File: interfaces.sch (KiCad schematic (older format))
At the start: 68 parts, among them J6 0878311420, J7 61300611121, U1 MTFC32GAPALBH-AIT, U14 XC7A100T-FGG484, U17 USB3300-EZK-TR, U18 USB3300-EZK-TR, U6 NVT2008DQ,115, Y1 TSX-3225, Y3 TSX-3225

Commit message: Replaced and connected eMMC, replaced RJ45
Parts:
- removed U1: MTFC32GAPALBH-AIT, antmicro-footprints:MICRON_EMMC_153, symbol antmicroMemory:MTFC32GAPALBH-AIT
- added U1: MTFC16GAPALNA-AIT, antmicro-footprints:BGA100CP100_17X10_1800X1400X140B46N, symbol antmicroMemory:MTFC16GAPALNA-AIT
- gave numbers to parts that had none: 1
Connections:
- wire segments 354 -> 358
- no-connect marks 11 -> 9
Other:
- note removed: "TODO: change to MTFC8GAMALNA which has 1mm ball pitch"
- moved on the sheet: C183, C184, C185, C186, C187, C188, C189, R116, R117, R118, R119, R120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

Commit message: Update RBIAS and filtering caps around ULPI USB controlers
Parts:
- removed C223, C224, C8, C9: C_4u7_0402, antmicro-footprints:0402-cap, symbol antmicroCapacitors0402:C_4u7_0402
- removed R5, R7: R_120k_0402, antmicro-footprints:0402-res, symbol antmicroResistors0402:R_120k_0402
- added R10, R11, R12, R9: R_0R_0402, antmicro-footprints:0402-res, symbol antmicroResistors0402:R_0R_0402
- added R5, R7: R_12k_0402, antmicro-footprints:0402-res, symbol antmicroResistors0402:R_12k_0402
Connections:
- wire segments 358 -> 345
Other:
- moved on the sheet: C22, C25, C26

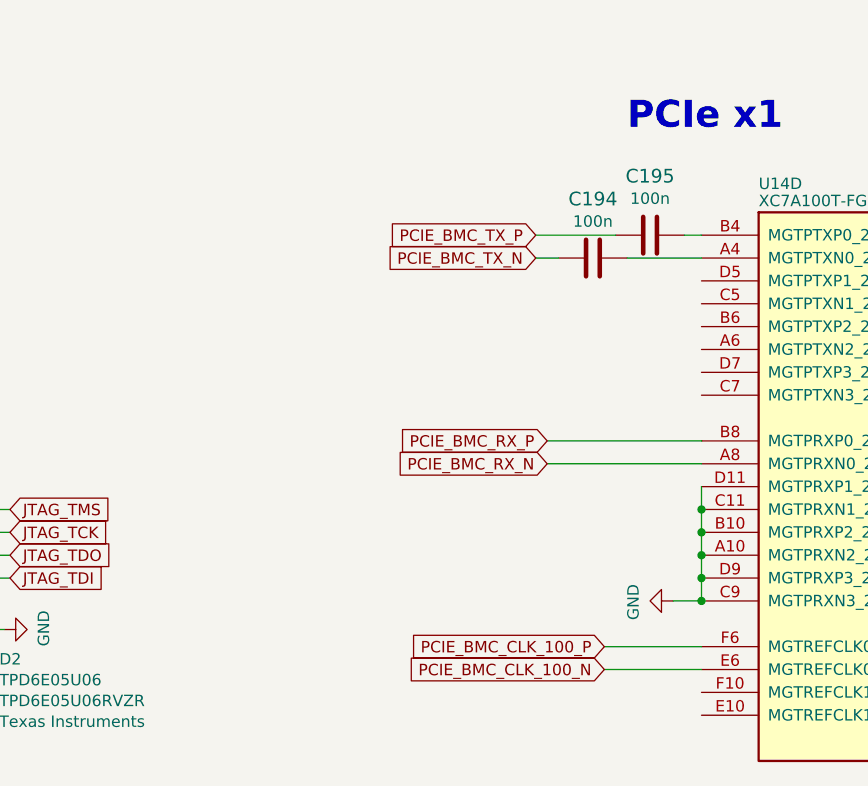
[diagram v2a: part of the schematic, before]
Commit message: DDR routing in progress
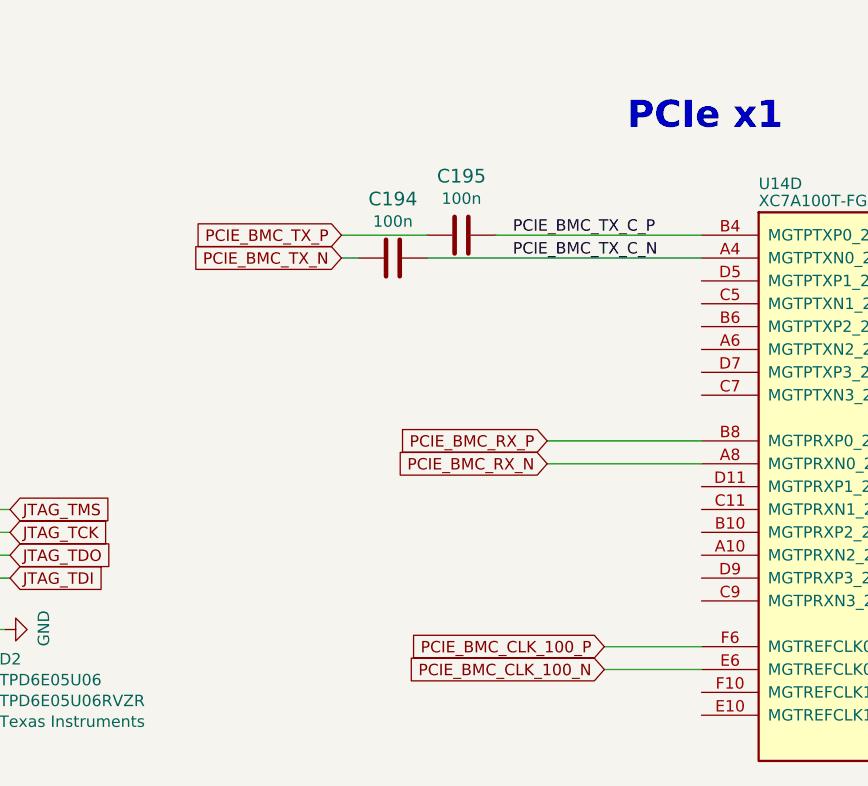
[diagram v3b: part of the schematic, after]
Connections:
- net GND: no longer U14.A10 (MGTPRXN2_216), U14.B10 (MGTPRXP2_216), U14.C11 (MGTPRXN1_216), U14.C9 (MGTPRXN3_216), U14.D11 (MGTPRXP1_216), U14.D9 (MGTPRXP3_216)
- net PCIE_BMC_TX_C_N: now reaches C194.1, U14.A4 (MGTPTXN0_216)
- net PCIE_BMC_TX_C_P: now reaches C195.1, U14.B4 (MGTPTXP0_216)
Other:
- moved on the sheet: C194, C195
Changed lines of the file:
@@
 L artix-dc-scm:C_100n_0402-artix-dc-scm C195
 U 1 1 604DDE71
-P 5750 1750
-F 0 "C195" V 5492 1750 60  0000 C CNN
-F 1 "C_100n_0402" H 5750 1600 60  0001 C CNN
-F 2 "artix-dc-scm-footprints:0402-cap" H 5950 1950 60  0001 L CNN
-F 3 "" H 5750 1750 50  0001 C CNN
-F 4 "Walsin" H 5950 2150 60  0001 L CNN "Manufacturer"
-F 5 "0402X104K6R3CT" H 5950 2050 60  0001 L CNN "MPN"
-F 6 "100n" V 5590 1750 50  0000 C CNN "Val"
-	1    5750 1750
+P 4925 1750
+F 0 "C195" V 4667 1750 60  0000 C CNN
+F 1 "C_100n_0402" H 4925 1600 60  0001 C CNN
+F 2 "artix-dc-scm-footprints:0402-cap" H 5125 1950 60  0001 L CNN
+F 3 "" H 4925 1750 50  0001 C CNN
+F 4 "Walsin" H 5125 2150 60  0001 L CNN "Manufacturer"
+F 5 "0402X104K6R3CT" H 5125 2050 60  0001 L CNN "MPN"
+F 6 "100n" V 4765 1750 50  0000 C CNN "Val"
+	1    4925 1750
 	0    1    1    0
 $EndComp
@@
 L artix-dc-scm:C_100n_0402-artix-dc-scm C194
 U 1 1 6050F852
-P 5500 1850
-F 0 "C194" V 5242 1850 60  0000 C CNN
-F 1 "C_100n_0402" H 5500 1700 60  0001 C CNN
-F 2 "artix-dc-scm-footprints:0402-cap" H 5700 2050 60  0001 L CNN
-F 3 "" H 5500 1850 50  0001 C CNN
-F 4 "Walsin" H 5700 2250 60  0001 L CNN "Manufacturer"
-F 5 "0402X104K6R3CT" H 5700 2150 60  0001 L CNN "MPN"
-F 6 "100n" V 5340 1850 50  0000 C CNN "Val"
-	1    5500 1850
+P 4625 1850
+F 0 "C194" V 4367 1850 60  0000 C CNN
+F 1 "C_100n_0402" H 4625 1700 60  0001 C CNN
+F 2 "artix-dc-scm-footprints:0402-cap" H 4825 2050 60  0001 L CNN
+F 3 "" H 4625 1850 50  0001 C CNN
+F 4 "Walsin" H 4825 2250 60  0001 L CNN "Manufacturer"
+F 5 "0402X104K6R3CT" H 4825 2150 60  0001 L CNN "MPN"
+F 6 "100n" V 4465 1850 50  0000 C CNN "Val"
+	1    4625 1850
 	0    1    1    0
 $EndComp
 Wire Wire Line
-	5900 1750 5975 1750
-Wire Wire Line
-	5600 1750 5250 1750
-Wire Wire Line
-	5250 1850 5350 1850
-Wire Wire Line
-	5650 1850 5975 1850
-Wire Wire Line
-	5975 2850 5975 2950
-Connection ~ 5975 2950
-Wire Wire Line
-	5975 2950 5975 3050
-Connection ~ 5975 3050
-Wire Wire Line
-	5975 3050 5975 3150
-Connection ~ 5975 3150
-Wire Wire Line
-	5975 3150 5975 3250
-Connection ~ 5975 3250
-Wire Wire Line
-	5975 3250 5975 3350
-Wire Wire Line
-	5975 3350 5850 3350
-Connection ~ 5975 3350
-$Comp
-L artix-dc-scm:GND-artix-dc-scm #PWR0122
-U 1 1 60C31F12
-P 5850 3350
-F 0 "#PWR0122" H 5850 3100 50  0001 C CNN
-F 1 "GND" H 5855 3177 50  0000 C CNN
-F 2 "" H 5850 3350 50  0001 C CNN
-F 3 "" H 5850 3350 50  0001 C CNN
-	1    5850 3350
-	0    1    1    0
-$EndComp
+	5075 1750 5975 1750
+Wire Wire Line
+	4775 1750 4400 1750
+Wire Wire Line
+	4400 1850 4475 1850
+Wire Wire Line
+	4775 1850 5975 1850
 Text Notes 7175 4900 0    118  ~ 24
 HPM SPI
@@
 Text GLabel 5550 3650 0    50   Input ~ 0
 PCIE_BMC_CLK_100_N
-Text GLabel 5250 1750 0    50   Input ~ 0
+Text GLabel 4400 1750 0    50   Input ~ 0
 PCIE_BMC_TX_P
-Text GLabel 5250 1850 0    50   Input ~ 0
+Text GLabel 4400 1850 0    50   Input ~ 0
 PCIE_BMC_TX_N
 Text GLabel 5300 2650 0    50   Input ~ 0
@@
 Wire Wire Line
 	10950 7100 10850 7100
+Text Label 5150 1750 0    50   ~ 0
+PCIE_BMC_TX_C_P
+Text Label 5150 1850 0    50   ~ 0
+PCIE_BMC_TX_C_N
 $EndSCHEMATC

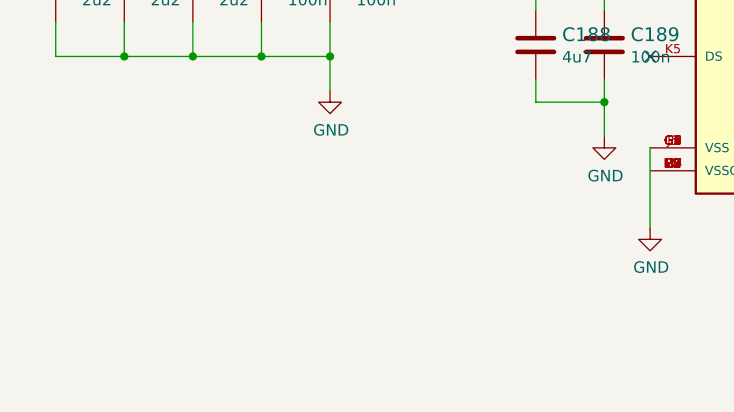
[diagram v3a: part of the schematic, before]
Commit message: Reconnect eMMC, route low speed signals
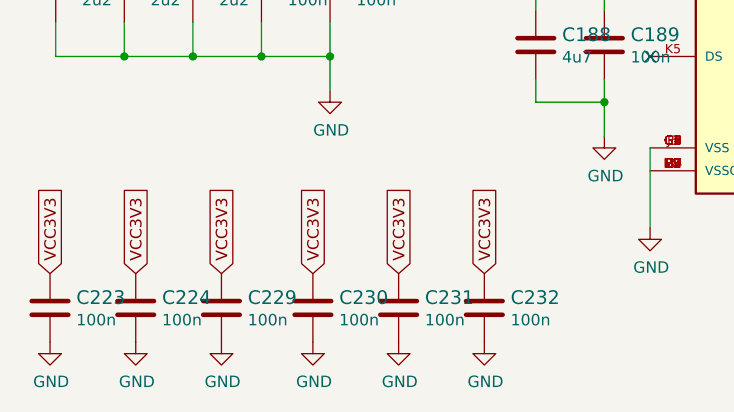
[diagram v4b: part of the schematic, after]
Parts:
- added C223, C224, C229, C230, C231, C232: C_100n_0402, artix-dc-scm-footprints:0402-cap, symbol artix-dc-scm:C_100n_0402-artix-dc-scm
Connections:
- net GND: now also C223.2, C224.2, C229.2, C230.2, C231.2, C232.2
- net VCC3V3: now also C223.1, C224.1, C229.1, C230.1, C231.1, C232.1
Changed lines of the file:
@@
 Text Label 5150 1850 0    50   ~ 0
 PCIE_BMC_TX_C_N
+$Comp
+L artix-dc-scm:C_100n_0402-artix-dc-scm C223
+U 1 1 6070CD97
+P 1375 10550
+F 0 "C223" H 1490 10595 60  0000 L CNN
+F 1 "C_100n_0402" H 1375 10400 60  0001 C CNN
+F 2 "artix-dc-scm-footprints:0402-cap" H 1575 10750 60  0001 L CNN
+F 3 "" H 1375 10550 50  0001 C CNN
+F 4 "Walsin" H 1575 10950 60  0001 L CNN "Manufacturer"
+F 5 "0402X104K6R3CT" H 1575 10850 60  0001 L CNN "MPN"
+F 6 "100n" H 1490 10497 50  0000 L CNN "Val"
+	1    1375 10550
+	1    0    0    -1
+$EndComp
+$Comp
+L artix-dc-scm:C_100n_0402-artix-dc-scm C224
+U 1 1 6070D63F
+P 1750 10550
+F 0 "C224" H 1865 10595 60  0000 L CNN
+F 1 "C_100n_0402" H 1750 10400 60  0001 C CNN
+F 2 "artix-dc-scm-footprints:0402-cap" H 1950 10750 60  0001 L CNN
+F 3 "" H 1750 10550 50  0001 C CNN
+F 4 "Walsin" H 1950 10950 60  0001 L CNN "Manufacturer"
+F 5 "0402X104K6R3CT" H 1950 10850 60  0001 L CNN "MPN"
+F 6 "100n" H 1865 10497 50  0000 L CNN "Val"
+	1    1750 10550
+	1    0    0    -1
+$EndComp
+$Comp
+L artix-dc-scm:C_100n_0402-artix-dc-scm C229
+U 1 1 6070D994
+P 2125 10550
+F 0 "C229" H 2240 10595 60  0000 L CNN
+F 1 "C_100n_0402" H 2125 10400 60  0001 C CNN
+F 2 "artix-dc-scm-footprints:0402-cap" H 2325 10750 60  0001 L CNN
+F 3 "" H 2125 10550 50  0001 C CNN
+F 4 "Walsin" H 2325 10950 60  0001 L CNN "Manufacturer"
+F 5 "0402X104K6R3CT" H 2325 10850 60  0001 L CNN "MPN"
+F 6 "100n" H 2240 10497 50  0000 L CNN "Val"
+	1    2125 10550
+	1    0    0    -1
+$EndComp
+$Comp
+L artix-dc-scm:GND-artix-dc-scm #PWR0123
+U 1 1 6070E02F
+P 2125 10700
+F 0 "#PWR0123" H 2125 10450 50  0001 C CNN
+F 1 "GND" H 2130 10527 50  0000 C CNN
+F 2 "" H 2125 10700 50  0001 C CNN
+F 3 "" H 2125 10700 50  0001 C CNN
+	1    2125 10700
+	1    0    0    -1
+$EndComp
+$Comp
+L artix-dc-scm:GND-artix-dc-scm #PWR0122
+U 1 1 6070E3A7
+P 1750 10700
+F 0 "#PWR0122" H 1750 10450 50  0001 C CNN
+F 1 "GND" H 1755 10527 50  0000 C CNN
+F 2 "" H 1750 10700 50  0001 C CNN
+F 3 "" H 1750 10700 50  0001 C CNN
+	1    1750 10700
+	1    0    0    -1
+$EndComp
+$Comp
+L artix-dc-scm:GND-artix-dc-scm #PWR0119
+U 1 1 6070E60A
+P 1375 10700
+F 0 "#PWR0119" H 1375 10450 50  0001 C CNN
+F 1 "GND" H 1380 10527 50  0000 C CNN
+F 2 "" H 1375 10700 50  0001 C CNN
+F 3 "" H 1375 10700 50  0001 C CNN
+	1    1375 10700
+	1    0    0    -1
+$EndComp
+Text GLabel 1375 10400 1    50   Input ~ 0
+VCC3V3
+Text GLabel 1750 10400 1    50   Input ~ 0
+VCC3V3
+Text GLabel 2125 10400 1    50   Input ~ 0
+VCC3V3
+$Comp
+L artix-dc-scm:C_100n_0402-artix-dc-scm C230
+U 1 1 6072F75C
+P 2525 10550
+F 0 "C230" H 2640 10595 60  0000 L CNN
+F 1 "C_100n_0402" H 2525 10400 60  0001 C CNN
+F 2 "artix-dc-scm-footprints:0402-cap" H 2725 10750 60  0001 L CNN
+F 3 "" H 2525 10550 50  0001 C CNN
+F 4 "Walsin" H 2725 10950 60  0001 L CNN "Manufacturer"
+F 5 "0402X104K6R3CT" H 2725 10850 60  0001 L CNN "MPN"
+F 6 "100n" H 2640 10497 50  0000 L CNN "Val"
+	1    2525 10550
+	1    0    0    -1
+$EndComp
+$Comp
+L artix-dc-scm:C_100n_0402-artix-dc-scm C231
+U 1 1 6072F765
+P 2900 10550
+F 0 "C231" H 3015 10595 60  0000 L CNN
+F 1 "C_100n_0402" H 2900 10400 60  0001 C CNN
+F 2 "artix-dc-scm-footprints:0402-cap" H 3100 10750 60  0001 L CNN
+F 3 "" H 2900 10550 50  0001 C CNN
+F 4 "Walsin" H 3100 10950 60  0001 L CNN "Manufacturer"
+F 5 "0402X104K6R3CT" H 3100 10850 60  0001 L CNN "MPN"
+F 6 "100n" H 3015 10497 50  0000 L CNN "Val"
+	1    2900 10550
+	1    0    0    -1
+$EndComp
+$Comp
+L artix-dc-scm:C_100n_0402-artix-dc-scm C232
+U 1 1 6072F76E
+P 3275 10550
+F 0 "C232" H 3390 10595 60  0000 L CNN
+F 1 "C_100n_0402" H 3275 10400 60  0001 C CNN
+F 2 "artix-dc-scm-footprints:0402-cap" H 3475 10750 60  0001 L CNN
+F 3 "" H 3275 10550 50  0001 C CNN
+F 4 "Walsin" H 3475 10950 60  0001 L CNN "Manufacturer"
+F 5 "0402X104K6R3CT" H 3475 10850 60  0001 L CNN "MPN"
+F 6 "100n" H 3390 10497 50  0000 L CNN "Val"
+	1    3275 10550
+	1    0    0    -1
+$EndComp
+$Comp
+L artix-dc-scm:GND-artix-dc-scm #PWR0126
+U 1 1 6072F774
+P 3275 10700
+F 0 "#PWR0126" H 3275 10450 50  0001 C CNN
+F 1 "GND" H 3280 10527 50  0000 C CNN
+F 2 "" H 3275 10700 50  0001 C CNN
+F 3 "" H 3275 10700 50  0001 C CNN
+	1    3275 10700
+	1    0    0    -1
+$EndComp
+$Comp
+L artix-dc-scm:GND-artix-dc-scm #PWR0125
+U 1 1 6072F77A
+P 2900 10700
+F 0 "#PWR0125" H 2900 10450 50  0001 C CNN
+F 1 "GND" H 2905 10527 50  0000 C CNN
+F 2 "" H 2900 10700 50  0001 C CNN
+F 3 "" H 2900 10700 50  0001 C CNN
+	1    2900 10700
+	1    0    0    -1
+$EndComp
+$Comp
+L artix-dc-scm:GND-artix-dc-scm #PWR0124
+U 1 1 6072F780
+P 2525 10700
+F 0 "#PWR0124" H 2525 10450 50  0001 C CNN
+F 1 "GND" H 2530 10527 50  0000 C CNN
+F 2 "" H 2525 10700 50  0001 C CNN
+F 3 "" H 2525 10700 50  0001 C CNN
+	1    2525 10700
+	1    0    0    -1
+$EndComp
+Text GLabel 2525 10400 1    50   Input ~ 0
+VCC3V3
+Text GLabel 2900 10400 1    50   Input ~ 0
+VCC3V3
+Text GLabel 3275 10400 1    50   Input ~ 0
+VCC3V3
 $EndSCHEMATC

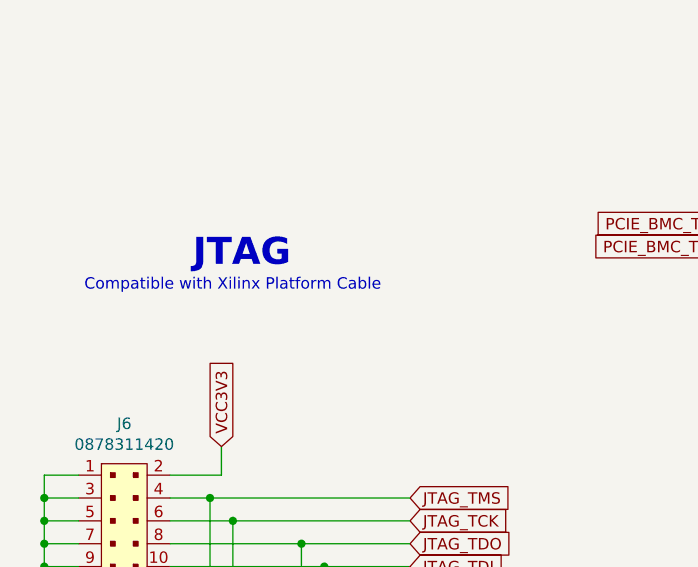
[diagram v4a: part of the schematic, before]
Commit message: Removed JTAG reference
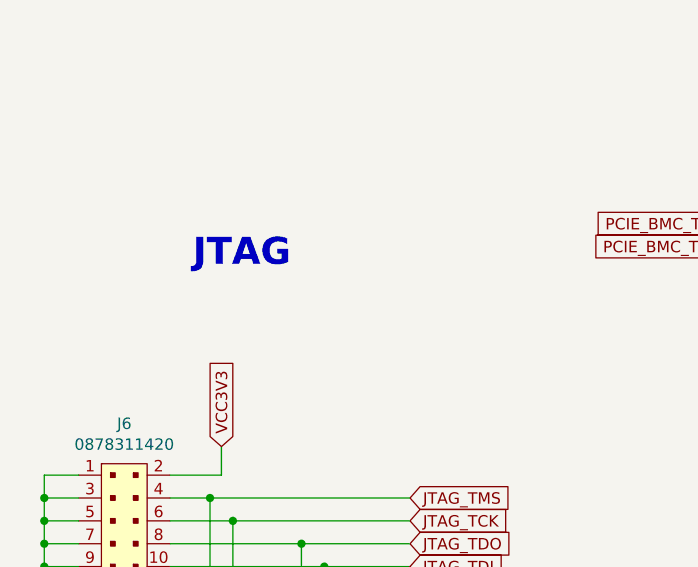
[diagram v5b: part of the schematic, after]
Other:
- note removed: "Compatible with Xilinx Platform Cable"
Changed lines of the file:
@@
 Wire Wire Line
 	2125 2850 2125 2725
-Text Notes 1525 2050 0    50   ~ 0
-Compatible with Xilinx Platform Cable
 Text GLabel 5700 5925 2    50   Input ~ 0
 I3C[0]_SCL

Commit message: Updated local libs
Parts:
- C10, C11, C12, C13, C18, C19, C20, C21, C22, C24, C25, C26: footprint antmicro-footprints:0402-cap -> artix-dc-scm-footprints:0402-cap; symbol antmicroCapacitors0402:C_100n_0402 -> artix-dc-scm:C_100n_0402
- C222, C23: footprint antmicro-footprints:0402-cap -> artix-dc-scm-footprints:0402-cap; symbol antmicroCapacitors0402:C_4u7_0402 -> artix-dc-scm:C_4u7_0402
- C4, C5, C6, C7: footprint antmicro-footprints:0402-cap -> artix-dc-scm-footprints:0402-cap; symbol antmicroCapacitors0402:C_12p_0402 -> artix-dc-scm:C_12p_0402
- R10, R11, R12, R9: footprint antmicro-footprints:0402-res -> artix-dc-scm-footprints:0402-res; symbol antmicroResistors0402:R_0R_0402 -> artix-dc-scm:R_0R_0402
- R3, R4: footprint antmicro-footprints:0402-res -> artix-dc-scm-footprints:0402-res; symbol antmicroResistors0402:R_1M5_0402 -> artix-dc-scm:R_1M5_0402
- R5, R7: footprint antmicro-footprints:0402-res -> artix-dc-scm-footprints:0402-res; symbol antmicroResistors0402:R_12k_0402 -> artix-dc-scm:R_12k_0402
- R6, R8: footprint antmicro-footprints:0402-res -> artix-dc-scm-footprints:0402-res; symbol antmicroResistors0402:R_1k_0402 -> artix-dc-scm:R_1k_0402
- U1: footprint antmicro-footprints:BGA100CP100_17X10_1800X1400X140B46N -> artix-dc-scm-footprints:BGA100CP100_17X10_1800X1400X140B46N; symbol antmicroMemory:MTFC16GAPALNA-AIT -> artix-dc-scm:MTFC16GAPALNA-AIT
- U17, U18: symbol antmicroInterfaceControllers:USB3300-EZK-TR -> artix-dc-scm:USB3300-EZK-TR
- Y1, Y3: footprint antmicro-footprints:KX-7 -> artix-dc-scm-footprints:KX-7; symbol antmicroCrystals:TSX-3225 -> artix-dc-scm:TSX-3225

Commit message: Local lib fix
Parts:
- U17, U18: footprint QFN50P500X500X100-33N -> artix-dc-scm-footprints:QFN50P500X500X100-33N
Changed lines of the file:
@@
 F 0 "U17" H 11325 4300 50  0000 C CNN
 F 1 "USB3300-EZK-TR" H 11600 4200 50  0000 C CNN
-F 2 "QFN50P500X500X100-33N" H 11700 3150 50  0001 L BNN
+F 2 "artix-dc-scm-footprints:QFN50P500X500X100-33N" H 11700 3150 50  0001 L BNN
 F 3 "" H 12200 3150 50  0001 L BNN
 F 4 "Microchip" H 12350 1850 50  0001 L BNN "Manufacturer"
@@
 F 0 "U18" H 11450 7825 50  0000 C CNN
 F 1 "USB3300-EZK-TR" H 11725 7725 50  0000 C CNN
-F 2 "QFN50P500X500X100-33N" H 11800 6650 50  0001 L BNN
+F 2 "artix-dc-scm-footprints:QFN50P500X500X100-33N" H 11800 6650 50  0001 L BNN
 F 3 "" H 12300 6650 50  0001 L BNN
 F 4 "Microchip" H 12450 5350 50  0001 L BNN "Manufacturer"

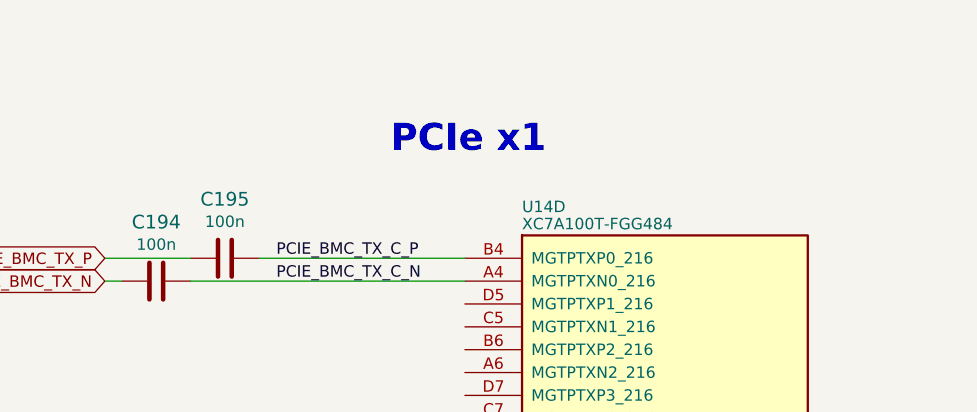
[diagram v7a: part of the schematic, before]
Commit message: Add FPGA 100MHz clock source
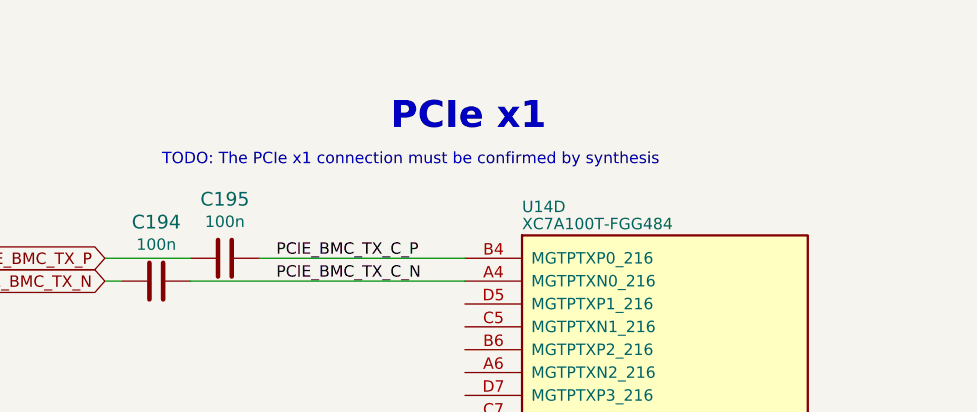
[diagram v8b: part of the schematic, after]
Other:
- note added: "TODO: The PCIe x1 connection must be confirmed by synthesis"
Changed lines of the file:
@@
 Text GLabel 6950 9050 2    50   Input ~ 0
 MMC_RSTN
-Text Notes 5650 1300 0    118  ~ 24
+Text Notes 5650 1200 0    118  ~ 24
 PCIe x1
 $Comp
@@
 Text GLabel 3275 10400 1    50   Input ~ 0
 VCC3V3
+Text Notes 4650 1350 0    50   ~ 0
+TODO: The PCIe x1 connection must be confirmed by synthesis
 $EndSCHEMATC
